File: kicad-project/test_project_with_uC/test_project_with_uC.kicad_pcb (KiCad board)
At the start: 2 copper layers, 1 part, among them U1 ATtiny2313-20SU

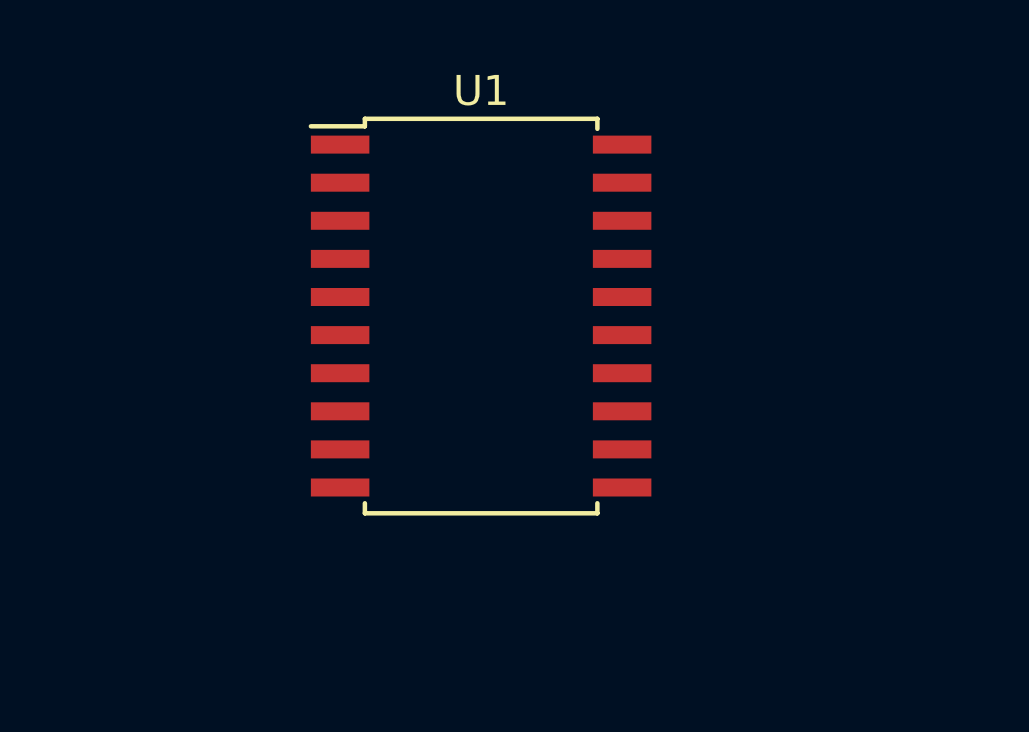
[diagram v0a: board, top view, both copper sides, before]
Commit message: add another microcontroller, for real world scene
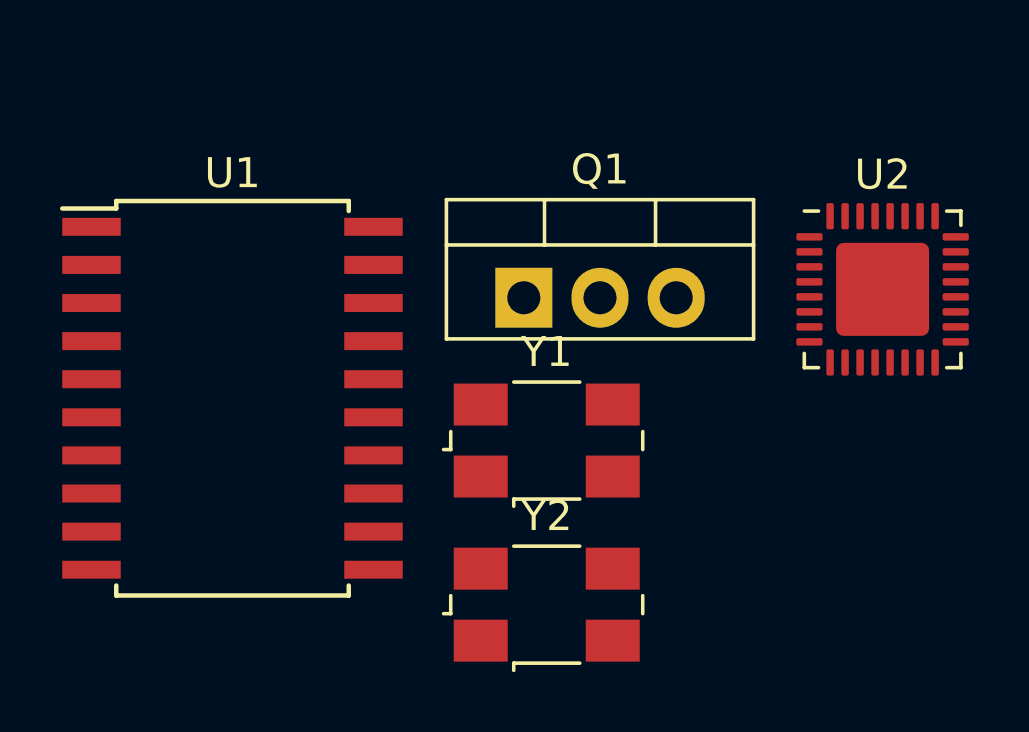
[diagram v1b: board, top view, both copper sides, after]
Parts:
- added Q1: IRF540N, Package_TO_SOT_THT:TO-220-3_Vertical, F.Cu at (155.7, 104.2)
- added U2: ATmega328-MU, Package_DFN_QFN:QFN-32-1EP_5x5mm_P0.5mm_EP3.1x3.1mm, F.Cu at (167.6, 104.0)
- added Y1: 12M, Crystal:Crystal_SMD_0603-4Pin_6.0x3.5mm, F.Cu at (156.4, 109.0)
- added Y2: 16M, Crystal:Crystal_SMD_0603-4Pin_6.0x3.5mm, F.Cu at (156.4, 114.5)
- moved U1 8.73 mm to (145.9, 107.6)
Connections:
- net Net-(U1-Pad1) renamed /~RST
- net Net-(U1-Pad11) renamed /~PPM_IN
- net Net-(U1-Pad12) renamed /CMP_IN
- net Net-(U1-Pad13) renamed /CMP_REF
- net Net-(U1-Pad14) renamed /MOTOR_A
- net Net-(U1-Pad15) renamed /MOTOR_B
- net Net-(U1-Pad16) renamed /BUZZER
- net Net-(U1-Pad6) renamed /WKUP0
- net Net-(U1-Pad7) renamed /ENCODER_A
- net Net-(U1-Pad8) renamed /SW_USR_1
- net Net-(U1-Pad9) renamed /SW_USR_2
- U1 pad 10: Net-(U1-Pad10) -> GND
- U1 pad 17: Net-(U1-Pad17) -> /MOSI
- U1 pad 18: Net-(U1-Pad18) -> /MISO
- U1 pad 19: Net-(U1-Pad19) -> /SCK
- U1 pad 2: Net-(U1-Pad2) -> /RXD
- U1 pad 20: Net-(U1-Pad20) -> +3V3
- U1 pad 3: Net-(U1-Pad3) -> /TXD
